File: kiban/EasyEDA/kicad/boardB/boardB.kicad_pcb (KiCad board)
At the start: 4 copper layers, 40 x 40 mm, 62 parts, among them J1 CHARGE, J2 AB1, J3 AB2, J4 BAT1, J5 BAT2, Q2 FS8205A_C908265, U1 BQ28Z620DRZR, U3 BQ25792RQMR

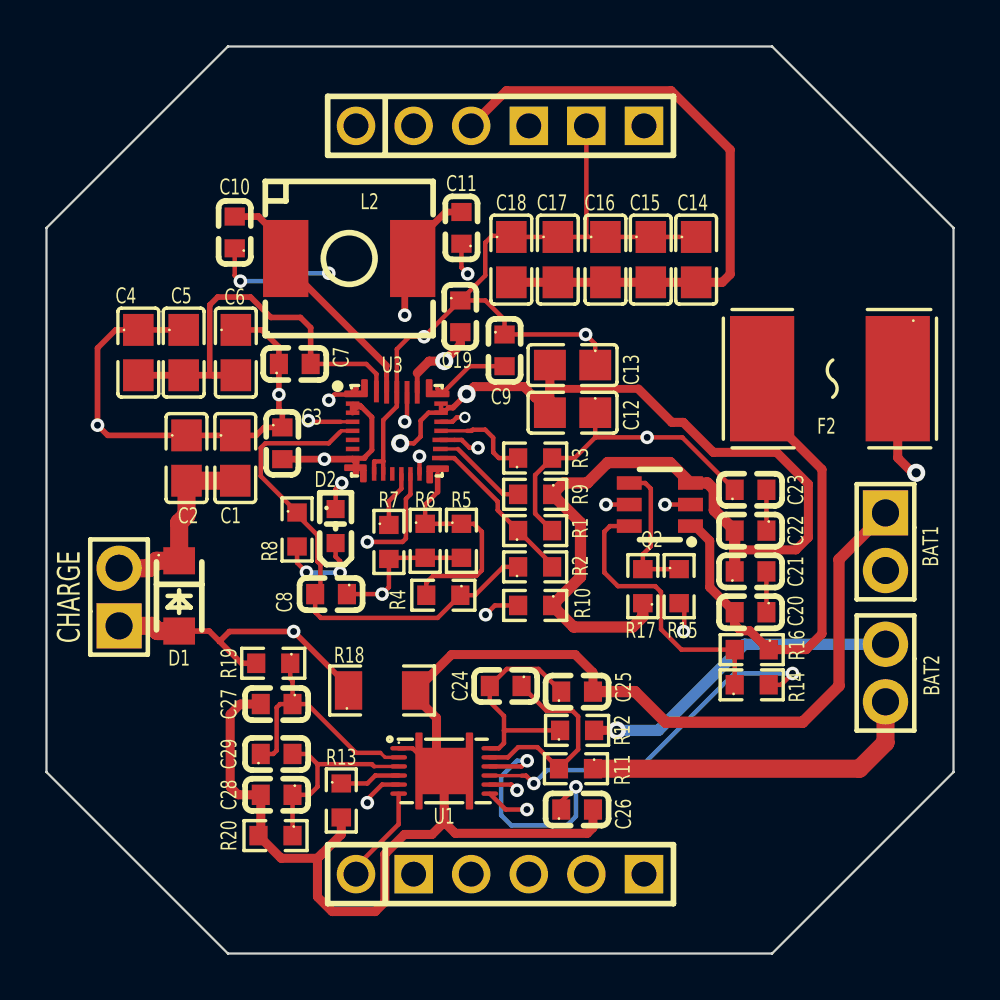
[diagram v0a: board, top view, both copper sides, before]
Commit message: feat: 基板B にテストピン (J10〜J14) を追加し、配線を修正。基板A の設定を更新
Co-Authored-By: Claude Opus 5.5 <noreply@anthropic.com>
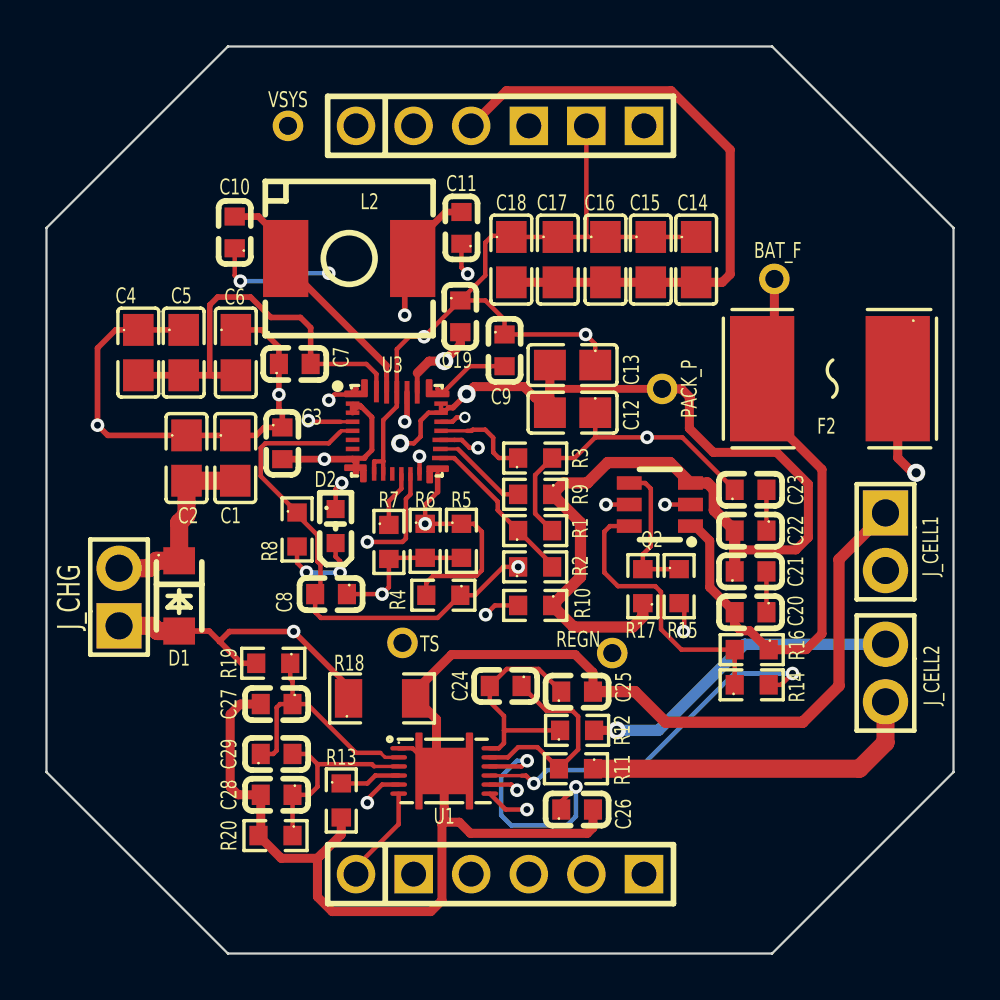
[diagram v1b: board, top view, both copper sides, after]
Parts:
- added J10: PACK_P, Connector_PinHeader_2.00mm:PinHeader_1x01_P2.00mm_Vertical, F.Cu at (7.15, -4.90)
- added J11: BAT_F, Connector_PinHeader_2.00mm:PinHeader_1x01_P2.00mm_Vertical, F.Cu at (12.1, -9.75)
- added J12: REGN, Connector_PinHeader_2.00mm:PinHeader_1x01_P2.00mm_Vertical, F.Cu at (4.95, 6.75)
- added J13: TS, Connector_PinHeader_2.00mm:PinHeader_1x01_P2.00mm_Vertical, F.Cu at (-4.30, 6.30)
- added J14: VSYS, Connector_PinHeader_2.00mm:PinHeader_1x01_P2.00mm_Vertical, F.Cu at (-9.35, -16.5)
- J1: value CHARGE -> J_CHG
- J4: value BAT1 -> J_CELL1
- J5: value BAT2 -> J_CELL2
- moved R18 0.35 mm to (-5.20, 8.75)
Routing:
- net REGN: track 22.8 -> 30.2 mm, vias 0 -> 1
- net TS: track 9.98 -> 15.6 mm, vias 0 -> 1
- net BAT_F: track 22.2 -> 26.8 mm
- net VSYS: track 48.3 -> 51.3 mm
- net PACK_P: track 57.2 -> 58.1 mm
- net BAT_N: track 70.7 -> 71.4 mm
